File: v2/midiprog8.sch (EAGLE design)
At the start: 56 parts, among them IC1 PIC18F4550_40, IC2 TPIC6B596N, IC3 78L05Z, IC4 TPIC6B596N, Q1 8MHz, Q2 2N2222A, Q3 2N2222A, Q4 2N2222A

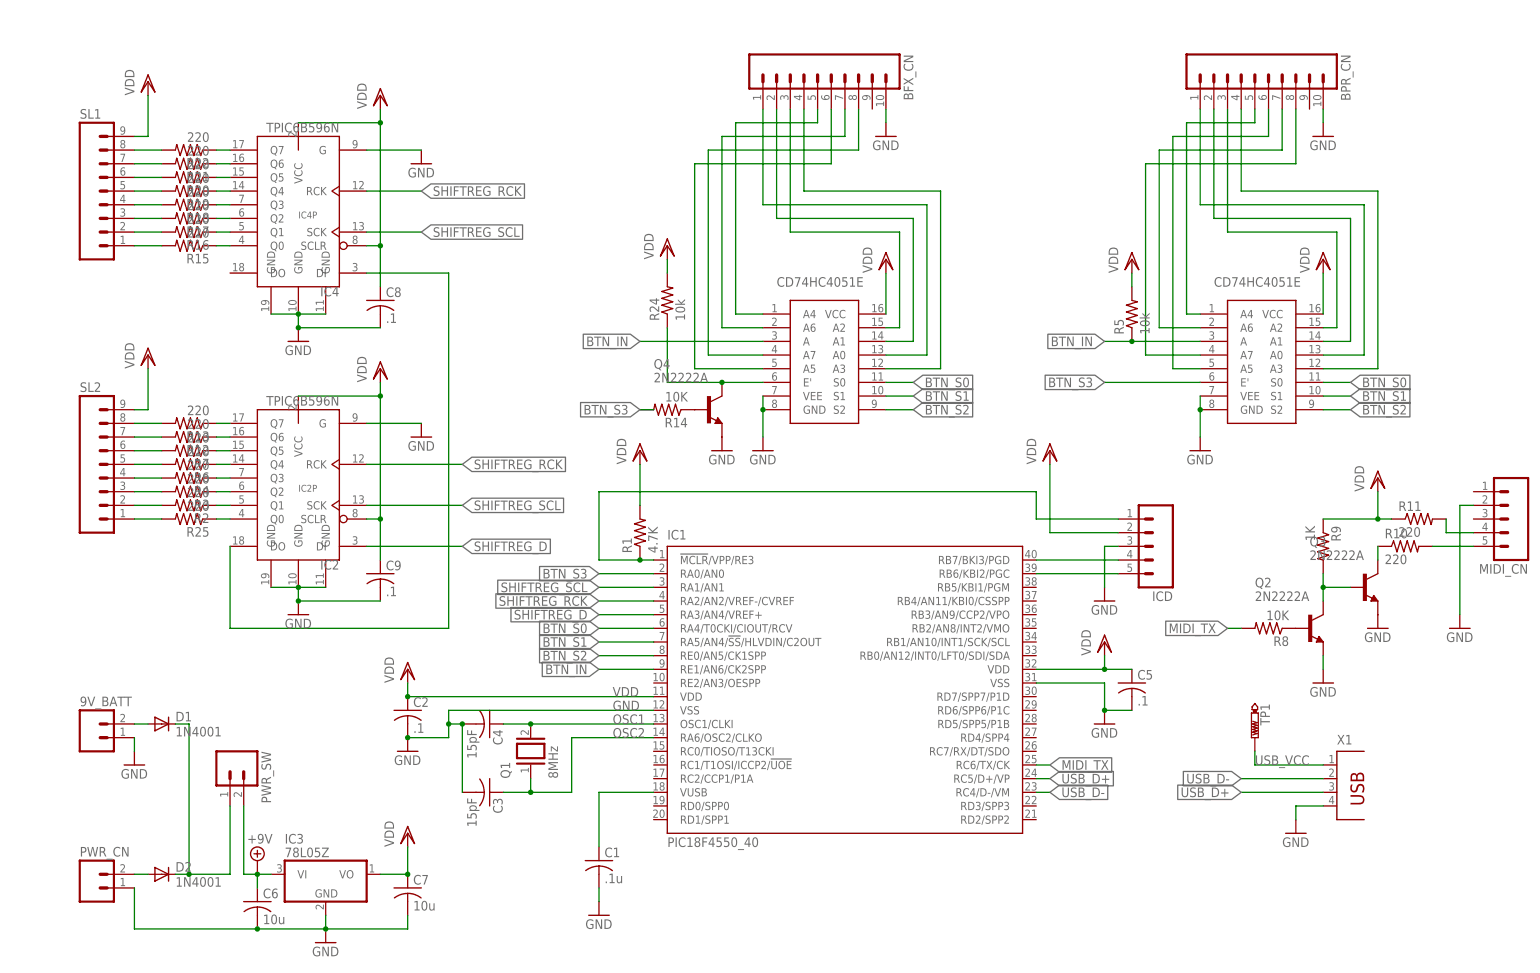
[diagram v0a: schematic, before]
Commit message: Put in dual row connectors for the ribbon cables
Every other pin in the ribbon will be ground to make it easier to wire.
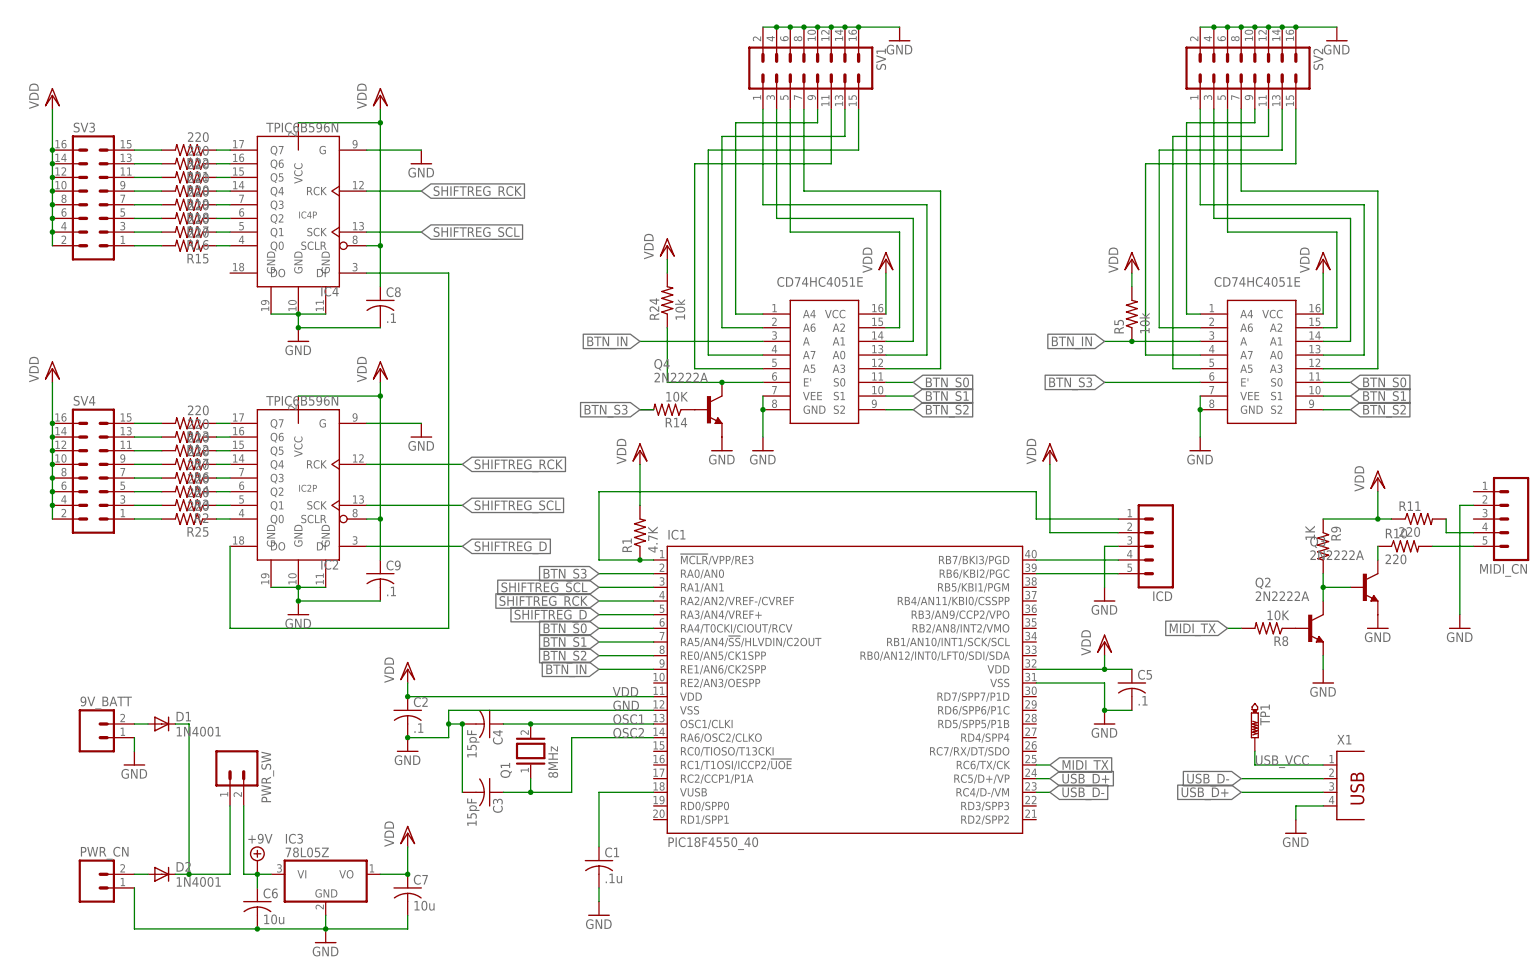
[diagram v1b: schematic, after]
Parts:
- removed BFX_CN, BPR_CN: (no value), con-amp-quick:M10
- removed SL1, SL2: (no value), con-amp-quick:M09
- added SV1, SV2, SV3, SV4: (no value), con-lstb:MA08-2
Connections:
- net BFX1: now also SV1.1; no longer BFX_CN.1
- net BFX2: now also SV1.3; no longer BFX_CN.2
- net BFX3: now also SV1.5; no longer BFX_CN.3
- net BFX4: now also SV1.7; no longer BFX_CN.4
- net BFX5: now also SV1.9; no longer BFX_CN.5
- net BFX6: now also SV1.11; no longer BFX_CN.6
- net BFX7: now also SV1.13; no longer BFX_CN.7
- net BFX8: now also SV1.15; no longer BFX_CN.8
- net BPR1: now also SV2.1; no longer BPR_CN.1
- net BPR2: now also SV2.3; no longer BPR_CN.2
- net BPR3: now also SV2.5; no longer BPR_CN.3
- net BPR4: now also SV2.7; no longer BPR_CN.4
- net BPR5: now also SV2.9; no longer BPR_CN.5
- net BPR6: now also SV2.11; no longer BPR_CN.6
- net BPR7: now also SV2.13; no longer BPR_CN.7
- net BPR8: now also SV2.15; no longer BPR_CN.8
- net GND: no longer BFX_CN.10, BPR_CN.10
- net N$11: now also SV3.13; no longer SL1.7
- net N$12: now also SV3.11; no longer SL1.6
- net N$19: now also SV3.9; no longer SL1.5
- net N$2: now also SV3.15; no longer SL1.8
- net N$20: now also SV3.7; no longer SL1.4
- net N$21: now also SV3.5; no longer SL1.3
- net N$22: now also SV3.3; no longer SL1.2
- net N$23: now also SV3.1; no longer SL1.1
- net N$24: now also SV4.13; no longer SL2.7
- net N$27: now also SV4.11; no longer SL2.6
- net N$28: now also SV4.9; no longer SL2.5
- net N$30: now also SV4.7; no longer SL2.4
- net N$32: now also SV4.5; no longer SL2.3
- net N$36: now also SV4.3; no longer SL2.2
- net N$37: now also SV4.1; no longer SL2.1
- net N$6: now also SV4.15; no longer SL2.8
- net VDD: now also SV3.10, SV3.12, SV3.14, SV3.16, SV3.2, SV3.4, SV3.6, SV3.8; no longer SL1.9, SL2.9

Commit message: Fixed warnings/errors; renamed connectors.
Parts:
- renumbered SV1 to BTN_FX_CN, SV2 to BTN_PR_CN, SV3 to LED_FX_CN, SV4 to LED_PR_CN
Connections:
- net GND: now also BTN_FX_CN.10, BTN_FX_CN.12, BTN_FX_CN.14, BTN_FX_CN.16, BTN_FX_CN.2, BTN_FX_CN.4, BTN_FX_CN.6, BTN_FX_CN.8, BTN_PR_CN.10, BTN_PR_CN.12, BTN_PR_CN.14, BTN_PR_CN.16, BTN_PR_CN.2, BTN_PR_CN.4, BTN_PR_CN.6, BTN_PR_CN.8
- net VDD: now also LED_PR_CN.10, LED_PR_CN.12, LED_PR_CN.14, LED_PR_CN.16, LED_PR_CN.2, LED_PR_CN.4, LED_PR_CN.6, LED_PR_CN.8
